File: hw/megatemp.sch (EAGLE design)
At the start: 30 parts, among them U1 STTS751, U2 STTS751, U3 STTS751, U4 STTS751, U5 STTS751, U6 STTS751, U7 STTS751, U8 STTS751

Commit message: Changed a name
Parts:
- renumbered JP1 to J1
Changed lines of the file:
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@@
 <part name="R11" library="resistor" deviceset="R-US_" device="R0402" value="22k"/>
 <part name="R12" library="resistor" deviceset="R-US_" device="R0402" value="22k"/>
-<part name="JP1" library="pinhead" deviceset="PINHD-2X16" device=""/>
+<part name="J1" library="pinhead" deviceset="PINHD-2X16" device=""/>
 <part name="R13" library="resistor" deviceset="R-US_" device="R0402" value="22k"/>
 <part name="R14" library="resistor" deviceset="R-US_" device="R0402" value="22k"/>
@@
 <instance part="R11" gate="G$1" x="45.72" y="53.34" rot="R90"/>
 <instance part="R12" gate="G$1" x="76.2" y="53.34" rot="R90"/>
-<instance part="JP1" gate="A" x="-50.8" y="30.48"/>
+<instance part="J1" gate="A" x="-50.8" y="30.48"/>
 <instance part="R13" gate="G$1" x="-7.62" y="35.56" rot="R90"/>
 <instance part="R14" gate="G$1" x="-7.62" y="12.7" rot="R90"/>
@@
 </segment>
 <segment>
-<pinref part="JP1" gate="A" pin="3"/>
+<pinref part="J1" gate="A" pin="3"/>
 <wire x1="-53.34" y1="45.72" x2="-66.04" y2="45.72" width="0.1524" layer="91"/>
 <label x="-58.42" y="45.72" size="1.778" layer="95" rot="MR0"/>
@@
 </segment>
 <segment>
-<pinref part="JP1" gate="A" pin="6"/>
+<pinref part="J1" gate="A" pin="6"/>
 <wire x1="-45.72" y1="43.18" x2="-30.48" y2="43.18" width="0.1524" layer="91"/>
 <label x="-40.64" y="43.18" size="1.778" layer="95"/>
@@
 </segment>
 <segment>
-<pinref part="JP1" gate="A" pin="28"/>
+<pinref part="J1" gate="A" pin="28"/>
 <wire x1="-45.72" y1="15.24" x2="-30.48" y2="15.24" width="0.1524" layer="91"/>
 <label x="-40.64" y="15.24" size="1.778" layer="95"/>
@@
 </segment>
 <segment>
-<pinref part="JP1" gate="A" pin="25"/>
+<pinref part="J1" gate="A" pin="25"/>
 <wire x1="-53.34" y1="17.78" x2="-66.04" y2="17.78" width="0.1524" layer="91"/>
 <label x="-58.42" y="17.78" size="1.778" layer="95" rot="MR0"/>
@@
 </segment>
 <segment>
-<pinref part="JP1" gate="A" pin="4"/>
+<pinref part="J1" gate="A" pin="4"/>
 <wire x1="-45.72" y1="45.72" x2="-22.86" y2="45.72" width="0.1524" layer="91"/>
 <label x="-40.64" y="45.72" size="1.778" layer="95"/>
@@
 </segment>
 <segment>
-<pinref part="JP1" gate="A" pin="32"/>
+<pinref part="J1" gate="A" pin="32"/>
 <wire x1="-45.72" y1="10.16" x2="-38.1" y2="10.16" width="0.1524" layer="91"/>
 <wire x1="-38.1" y1="10.16" x2="-38.1" y2="5.08" width="0.1524" layer="91"/>
 <wire x1="-38.1" y1="5.08" x2="-60.96" y2="5.08" width="0.1524" layer="91"/>
 <wire x1="-60.96" y1="5.08" x2="-60.96" y2="10.16" width="0.1524" layer="91"/>
-<pinref part="JP1" gate="A" pin="31"/>
+<pinref part="J1" gate="A" pin="31"/>
 <wire x1="-60.96" y1="10.16" x2="-53.34" y2="10.16" width="0.1524" layer="91"/>
 <label x="-40.64" y="10.16" size="1.778" layer="95"/>

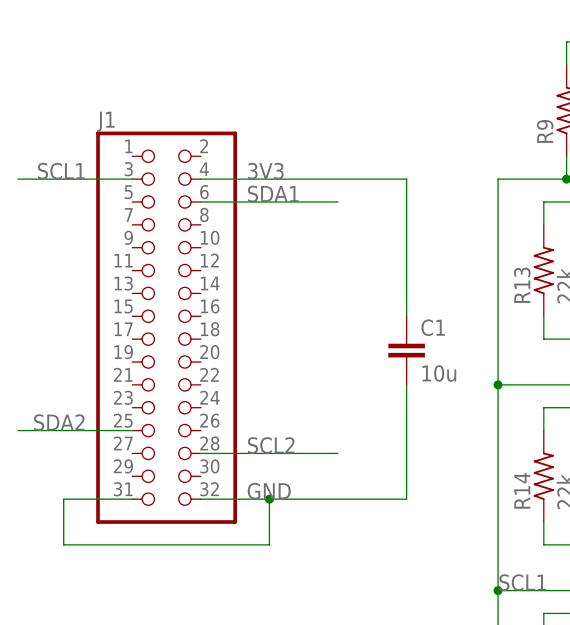
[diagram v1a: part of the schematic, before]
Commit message: Updated design to a functional schematic
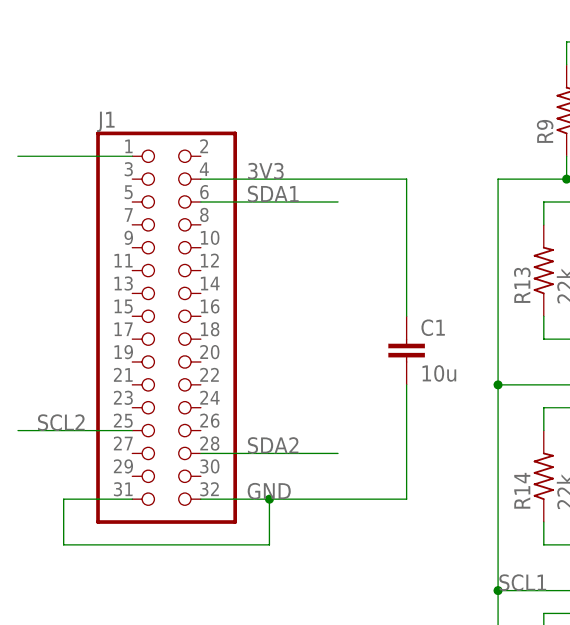
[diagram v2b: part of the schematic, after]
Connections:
- net SCL1: now also J1.1; no longer J1.3
- net SCL2: now also J1.25; no longer J1.28
- net SDA2: now also J1.28; no longer J1.25
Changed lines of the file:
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@@
 </segment>
 <segment>
-<pinref part="J1" gate="A" pin="3"/>
-<wire x1="-53.34" y1="45.72" x2="-66.04" y2="45.72" width="0.1524" layer="91"/>
-<label x="-58.42" y="45.72" size="1.778" layer="95" rot="MR0"/>
+<pinref part="J1" gate="A" pin="1"/>
+<wire x1="-53.34" y1="48.26" x2="-66.04" y2="48.26" width="0.1524" layer="91"/>
 </segment>
 </net>
@@
 </segment>
 <segment>
-<pinref part="J1" gate="A" pin="28"/>
-<wire x1="-45.72" y1="15.24" x2="-30.48" y2="15.24" width="0.1524" layer="91"/>
-<label x="-40.64" y="15.24" size="1.778" layer="95"/>
+<pinref part="J1" gate="A" pin="25"/>
+<wire x1="-53.34" y1="17.78" x2="-66.04" y2="17.78" width="0.1524" layer="91"/>
+<label x="-58.42" y="17.78" size="1.778" layer="95" rot="MR0"/>
 </segment>
 </net>
@@
 </segment>
 <segment>
-<pinref part="J1" gate="A" pin="25"/>
-<wire x1="-53.34" y1="17.78" x2="-66.04" y2="17.78" width="0.1524" layer="91"/>
-<label x="-58.42" y="17.78" size="1.778" layer="95" rot="MR0"/>
+<pinref part="J1" gate="A" pin="28"/>
+<wire x1="-45.72" y1="15.24" x2="-30.48" y2="15.24" width="0.1524" layer="91"/>
+<label x="-40.64" y="15.24" size="1.778" layer="95"/>
 </segment>
 </net>
